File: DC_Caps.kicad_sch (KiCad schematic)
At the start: 19 parts

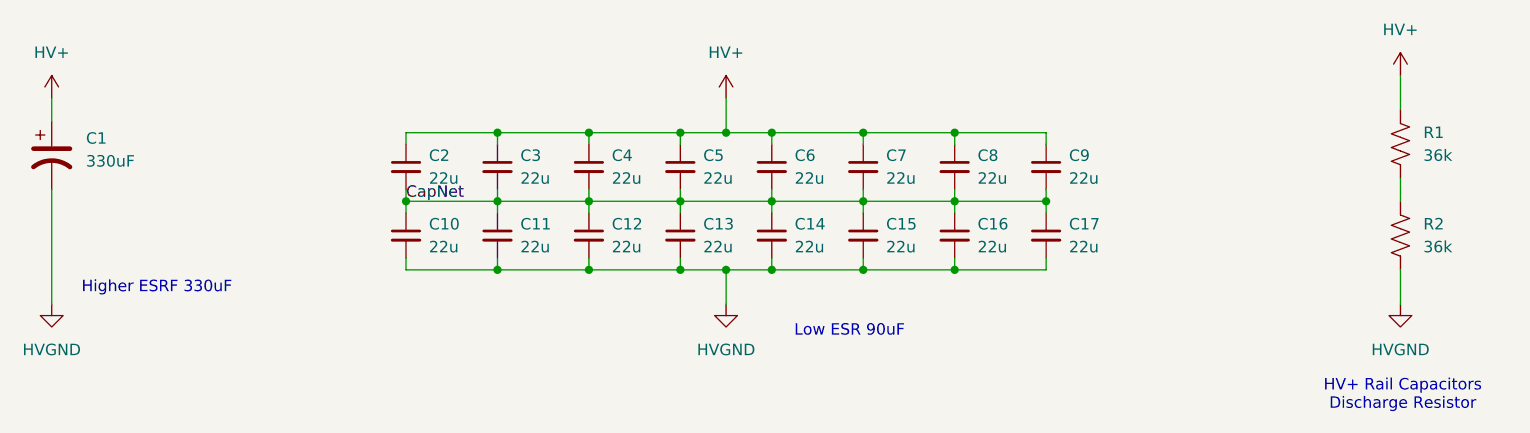
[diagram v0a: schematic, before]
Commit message: new bulk caps, new HV+,- connector placement
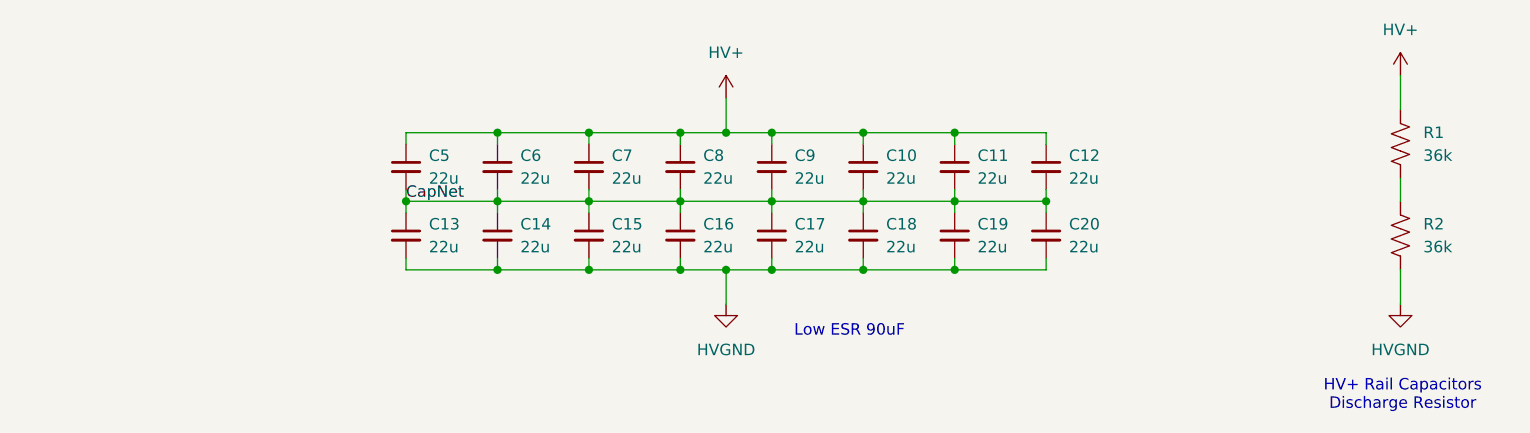
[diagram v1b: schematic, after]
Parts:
- removed C1: 330uF, TractionInverter:CAPPRD750W80D1825H4150, symbol Device:C_Polarized_US
- renumbered C7 to C10, C8 to C11, C9 to C12, C10 to C13, C11 to C14, C12 to C15, C13 to C16, C14 to C17, C15 to C18, C16 to C19, C17 to C20, C2 to C5, C3 to C6, C4 to C7, C5 to C8, C6 to C9
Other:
- note removed: "Higher ESRF 330uF"

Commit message: killed testpoints
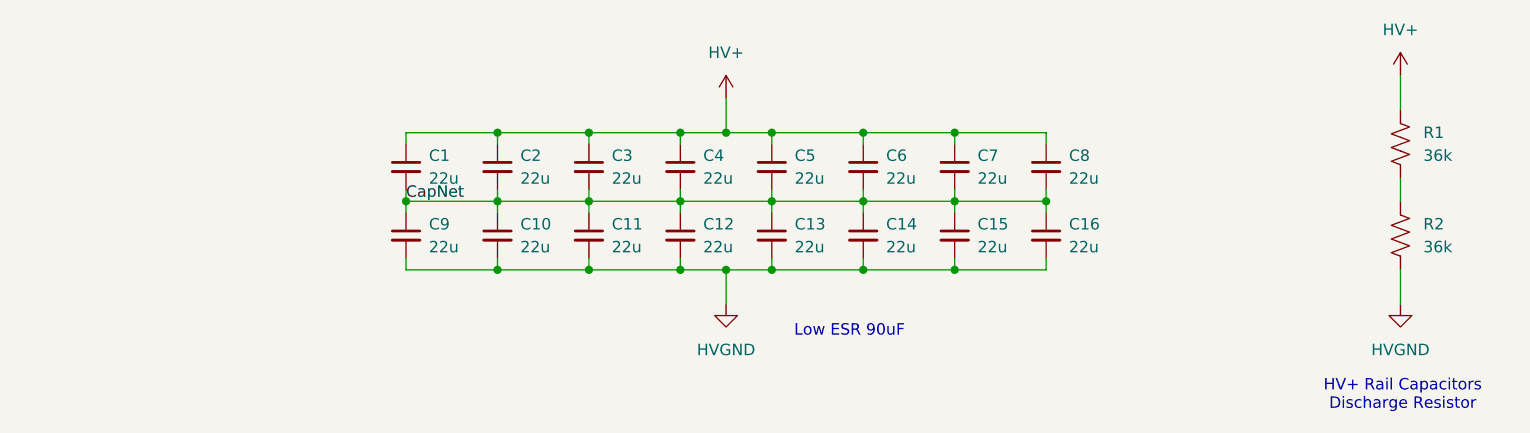
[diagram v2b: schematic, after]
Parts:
- renumbered C5 to C1, C14 to C10, C15 to C11, C16 to C12, C17 to C13, C18 to C14, C19 to C15, C20 to C16, C6 to C2, C7 to C3, C8 to C4, C9 to C5, C10 to C6, C11 to C7, C12 to C8, C13 to C9
